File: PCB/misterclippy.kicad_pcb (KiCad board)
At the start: 2 copper layers, 30.2 x 109.2 mm, 73 parts, among them J1 PWR, J2 Output Gate, J3 Output Gate, J4 Input, J5 Input, J6 Audio In, J7 Through, J8 Audio In, J9 Through, Q1 BC547, Q2 BC547, U1 LM393, U2 TL072, U3 LM393, U4 TL072, U5 LM393

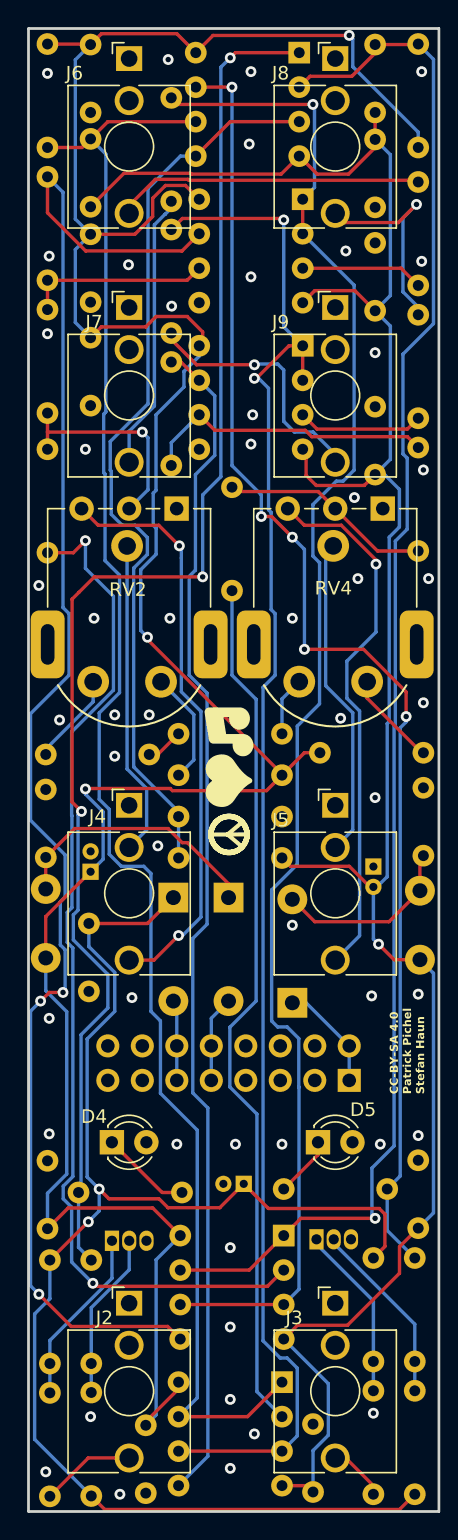
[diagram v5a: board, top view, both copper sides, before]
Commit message: Adapt PCB to fixed schematic
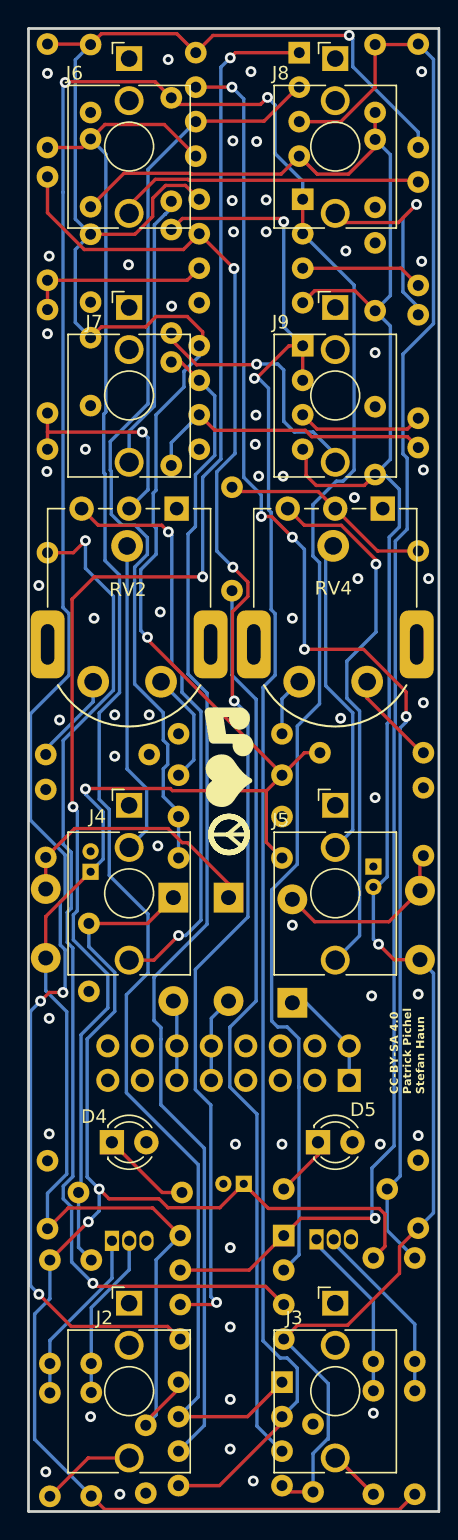
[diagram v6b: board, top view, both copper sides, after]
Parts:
- R1, R2: value 10M -> 1M
- R12, R7: value 10k -> 4k7
- R14, R9: value 10k -> 1k
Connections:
- R20 pad 1: Net-(U3A--) -> Net-(U3A-+)
- R22 pad 1: Net-(U3B-+) -> Net-(U3B-_)
- R25 pad 1: Net-(U5A--) -> Net-(U5A-+)
- R27 pad 1: Net-(U5B-+) -> Net-(U5B-_)
- R4 pad 2: -12V -> +12V
- U1 pad 2: /Detector 1/Clipped -> DELAY_THRESHOLD
- U1 pad 3: DELAY_THRESHOLD -> /Detector 1/Clipped
- U1 pad 5: DELAY_THRESHOLD -> /Detector 2/Clipped
- U1 pad 6: /Detector 2/Clipped -> DELAY_THRESHOLD
- U2 pad 7: Net-(U3B-+) -> Net-(U3B-_)
- U3 pad 2: Net-(U3A--) -> Net-(U2A--)
- U3 pad 3: Net-(U2A--) -> Net-(U3A-+)
- U3 pad 5: Net-(U3B-+) -> Net-(U2A--)
- U3 pad 6: Net-(U2A--) -> Net-(U3B-_)
- U4 pad 7: Net-(U5B-+) -> Net-(U5B-_)
- U5 pad 2: Net-(U5A--) -> Net-(U4A--)
- U5 pad 3: Net-(U4A--) -> Net-(U5A-+)
- U5 pad 5: Net-(U5B-+) -> Net-(U4A--)
- U5 pad 6: Net-(U4A--) -> Net-(U5B-_)
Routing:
- net Net-(U3B-+): track 114.6 -> 0.00 mm, vias 3 -> 0
- net Net-(U3B-_): track 0.00 -> 102.7 mm, vias 0 -> 4
- net Net-(U2A--): track 113.5 -> 215.4 mm, vias 1 -> 5
- net Net-(U5B-+): track 87.6 -> 0.00 mm
- net Net-(U5B-_): track 0.00 -> 87.3 mm
- net Net-(U3A-+): track 0.00 -> 76.7 mm, vias 0 -> 2
- net Net-(U3A--): track 76.2 -> 0.00 mm, vias 2 -> 0
- net Net-(U5A-+): track 0.00 -> 66.5 mm
- net Net-(U5A--): track 64.0 -> 0.00 mm
- net -12V: track 165.5 -> 158.0 mm
- net +12V: track 201.3 -> 206.8 mm
- net GND: track 3.40 -> 0.00 mm, vias 52 -> 57
- net /Detector 1/Clipped: track 115.6 -> 118.1 mm
- net DELAY_THRESHOLD: track 67.1 -> 69.1 mm
- net /Detector 2/Clipped: track 120.7 -> 121.9 mm

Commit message: Bump PCB revision number to v1.1
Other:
- board text added: "v1.1"
- board text removed: "v1"
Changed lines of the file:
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@@
   (gr_line locked (start 104.671 160.147) (end 134.851 160.147)
     (stroke (width 0.2) (type solid)) (layer "Edge.Cuts"))
-  (gr_text "v1" (at 110.109 131.318) (layer "B.SilkS")
-    (effects (font (size 0.6 0.6) (thickness 0.1) bold) (justify left bottom mirror))
+  (gr_text "v1.1" (at 109.1 131.3) (layer "B.SilkS")
+    (effects (font (size 0.6 0.6) (thickness 0.1) bold) (justify right bottom mirror))
   )
   (gr_text "Red Stripe -12V" (at 132.715 122.682 90) (layer "B.SilkS")

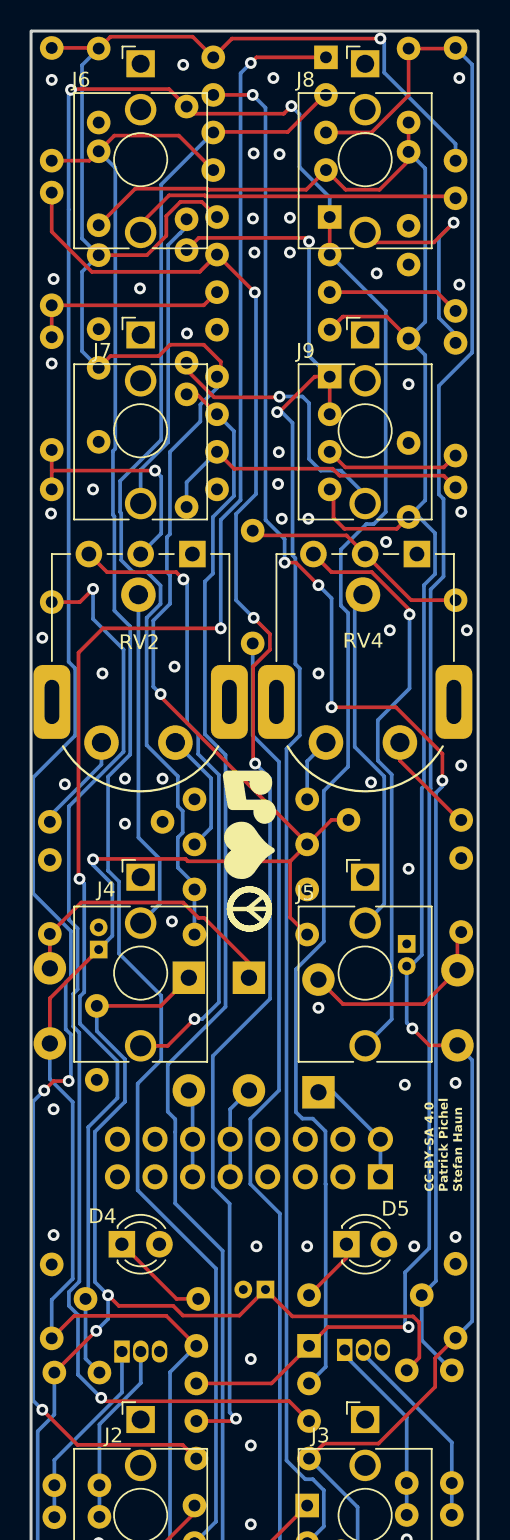
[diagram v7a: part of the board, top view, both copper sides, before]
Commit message: :art: Apply geographical reannotation
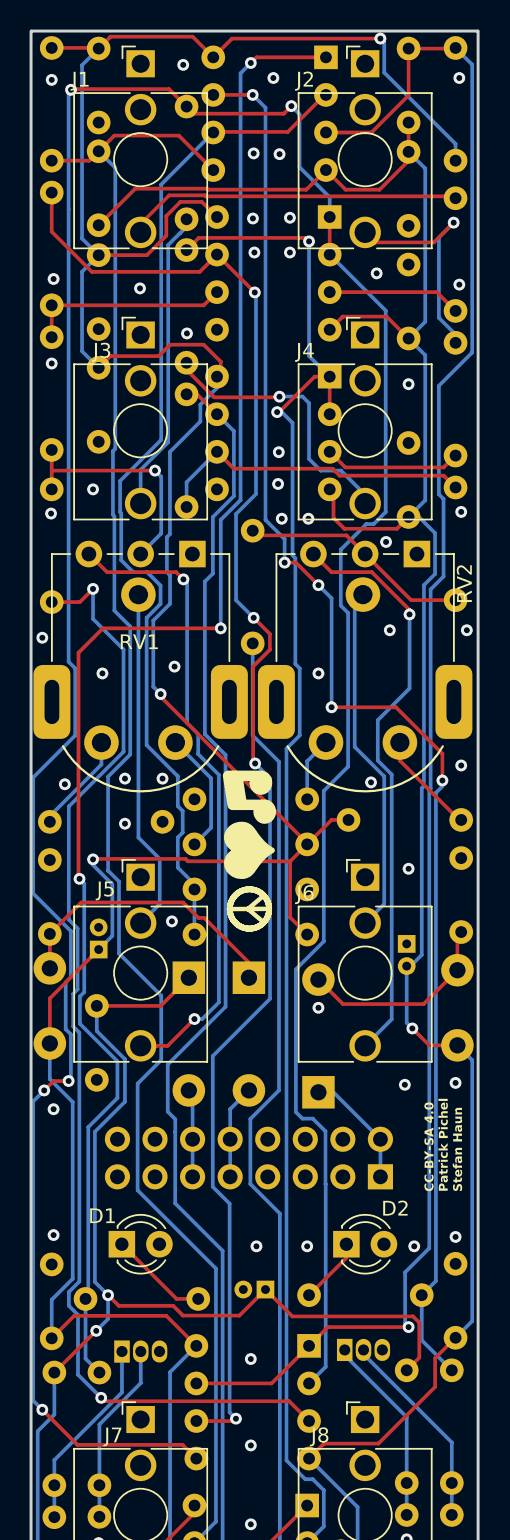
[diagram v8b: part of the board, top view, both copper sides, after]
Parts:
- renumbered C7 to C1, C6 to C10, C5 to C11, C2 to C12, C1 to C13, C4 to C15, C13 to C16, C18 to C17, C17 to C18, C9 to C2, C8 to C3, C10 to C4, C12 to C5, C11 to C6, C15 to C7, C16 to C8, C3 to C9, D4 to D1, D5 to D2, D2 to D3, D1 to D4, D3 to D5, FB2 to FB1, FB1 to FB2, J6 to J1, J8 to J2, J7 to J3, J9 to J4, J4 to J5, J5 to J6, J2 to J7, J3 to J8, J1 to J9, Q2 to Q1, Q1 to Q2, R2 to R1, R26 to R10, R20 to R11, R25 to R12, R18 to R13, R17 to R14, R16 to R15, R15 to R16, R3 to R17, R4 to R18, R10 to R19, R1 to R2, R5 to R20, R13 to R21, R8 to R22, R12 to R23, R7 to R24, R14 to R25, R9 to R26, R11 to R27, R6 to R28, R19 to R3, R22 to R4, R23 to R5, R24 to R6, R21 to R7, R28 to R8, R27 to R9, RV2 to RV1, RV4 to RV2, RV1 to RV4, U4 to U3, U3 to U4
